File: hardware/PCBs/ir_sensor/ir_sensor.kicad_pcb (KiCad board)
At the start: 2 copper layers, 45.5 x 71 mm, 32 parts, among them J1 Conn_01x04, J10 Conn_01x02, J11 Conn_01x02, J12 Conn_01x02, J13 Conn_01x02, J2 Conn_01x04, J3 Conn_01x04, J4 Conn_01x02, J5 Conn_01x02, J6 Conn_01x02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

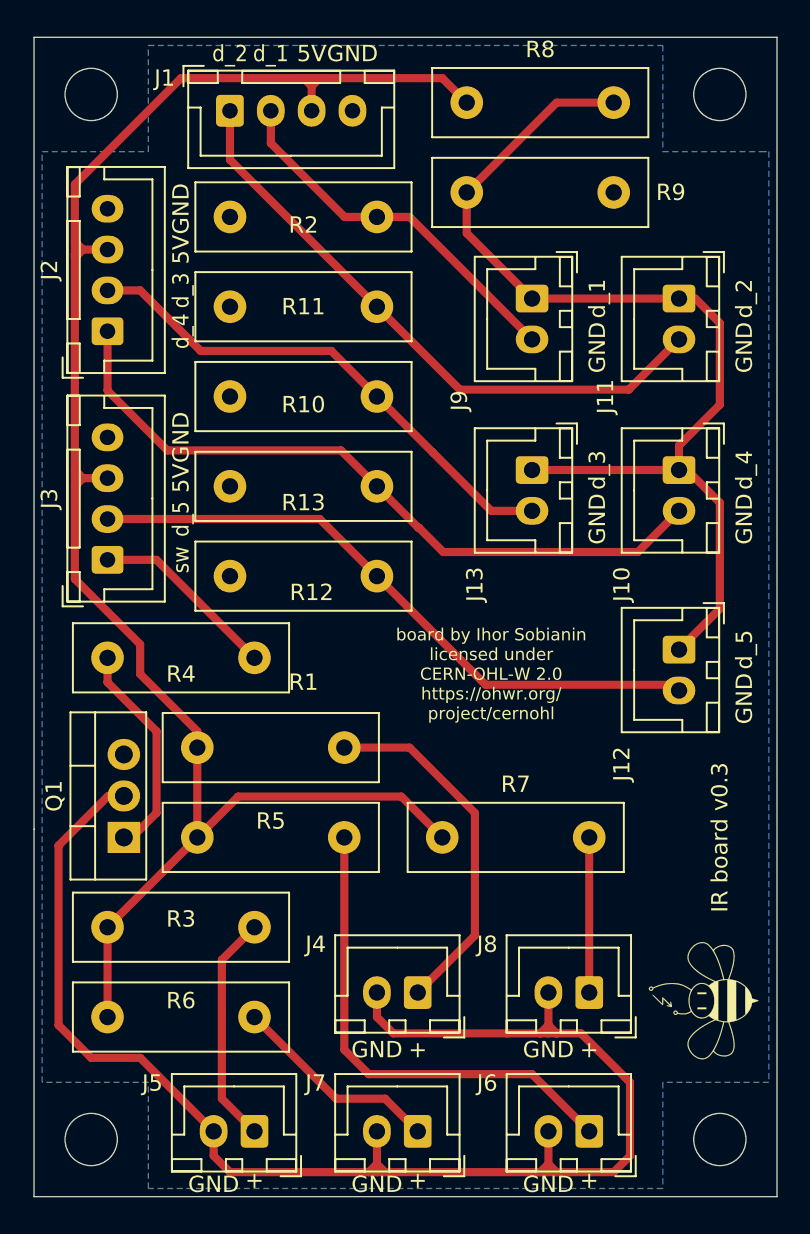
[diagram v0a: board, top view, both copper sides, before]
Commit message: Update IR sensor to v0.4
IR sensor board updated to version 0.4:
- removed MOSFET switch;
First of all, it was supposed to be IRFL44 , L version which can be used with logic levels. But instead we put IRFZ which barely opens at 3.3 V and thus cannot be effectively used here. Moreover, during the actual usage of the board, 5V line was constantly ON and it did not cause to much of a trouble. This change is also correlated with the upcoming redesign of the main hub.
- Add additional phototransistor connector
- Add additional IR LED connector

Co-Authored-By: Andre Maia Chagas <a.maia-chagas@sussex.ac.uk>
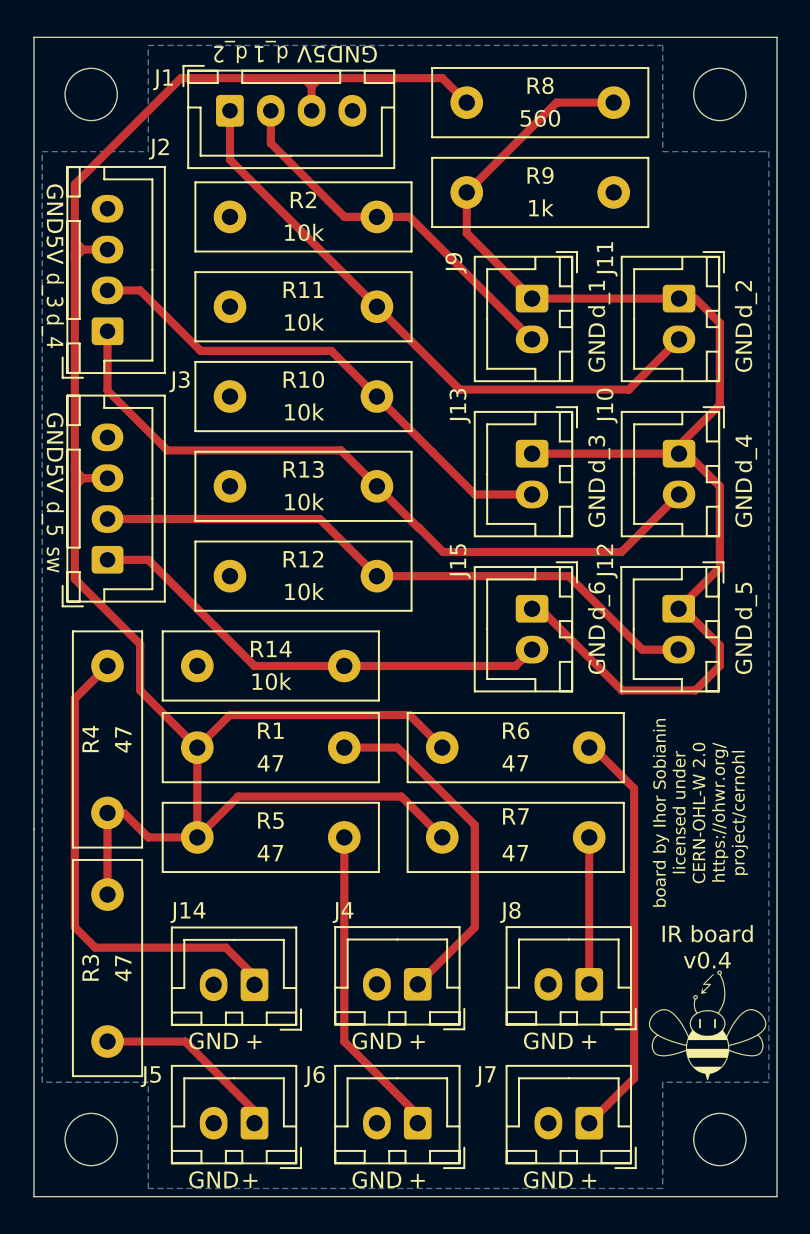
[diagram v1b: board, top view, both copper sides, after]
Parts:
- removed Q1: IRFZ24NPBF, Package_TO_SOT_THT:TO-220-3_Vertical
- added J14: Conn_01x02, Connector_JST:JST_XH_B2B-XH-A_1x02_P2.50mm_Vertical, F.Cu at (95.5, 83.5)
- added J15: Conn_01x02, Connector_JST:JST_XH_B2B-XH-A_1x02_P2.50mm_Vertical, F.Cu at (112.5, 60.5)
- added R14: 10k, Resistor_THT:R_Box_L13.0mm_W4.0mm_P9.00mm, F.Cu at (101.0, 64.0)
- moved R6 26.3 mm to (107.0, 69.0)
- moved J6 10.5 mm to (105.5, 92.0)
- moved J7 10.5 mm to (116.0, 92.0)
- moved R4 9.01 mm to (86.5, 64.0), turned to -90 degrees
- moved J12 2.50 mm to (121.5, 60.5)
- moved R3 2.00 mm to (86.5, 78.0), turned to -90 degrees
- moved G*** 1.52 mm to (123.2, 86.0), turned to 0 degrees
- moved J10 1.00 mm to (121.5, 51.0)
- moved J13 1.00 mm to (112.5, 51.0)
- moved J4 0.50 mm to (105.5, 83.5)
- moved J5 0.50 mm to (95.5, 92.0)
- moved J8 0.50 mm to (116.0, 83.5)
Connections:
- J3 pad 1: sw_led -> d_6
- J4 pad 2: Vdrive -> GND
- J5 pad 2: Vdrive -> GND
- J6 pad 2: Vdrive -> GND
- J7 pad 2: Vdrive -> GND
- J8 pad 2: Vdrive -> GND
- R4 pad 1: sw_led -> Net-(R4-Pad1)
- R4 pad 2: Net-(Q1-Pad1) -> +5V
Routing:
- net Vdrive: track 91.7 -> 0.00 mm
- net Net-(R4-Pad1): track 0.00 -> 29.6 mm
- net d_6: track 0.00 -> 29.1 mm
- net +3V3: track 64.0 -> 80.4 mm
- net +5V: track 109.8 -> 124.3 mm
- net Net-(Q1-Pad1): track 13.4 -> 0.00 mm
- net Net-(J7-Pad1): track 12.9 -> 25.5 mm
- net sw_led: track 11.5 -> 0.00 mm
- net Net-(J6-Pad1): track 30.1 -> 19.4 mm
- net Net-(J5-Pad1): track 14.2 -> 11.5 mm
- net d_5: track 39.3 -> 38.3 mm
- net Net-(J4-Pad1): track 22.1 -> 21.2 mm
- net Net-(J8-Pad1): track 9.50 -> 9.00 mm
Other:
- board text added: "IR board v0.4"
- board text added: "d_6"
- board text removed: "IR board v0.3"
